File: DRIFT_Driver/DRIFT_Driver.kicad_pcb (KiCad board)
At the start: 2 copper layers, 93 parts, among them IC1 DRV8313RHHR, IC2 DRV8313RHHR, IC4 ESP32-S3-WROOM-1-N4, J1 USB4105-GF-A, J2 Conn_01x04, J3 Conn_01x06, J4 Conn_01x06, J5 Conn_01x04, J6 Conn_01x02, J7 Conn_01x03, J8 Conn_01x03, SW1 SW_SPST, SW2 SW_SPST, U1 74HC32, U2 INA199xxDCK, U3 INA199xxDCK, U4 74HC32, U5 INA199xxDCK, U6 INA199xxDCK, U8 USBLC6-2SC6, U9 MIC5365-3.3YC5

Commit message: Fixed some 3d models
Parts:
- removed the C3 at (124.1, 63.2)
- added C23: 10u, Capacitor_SMD:C_0805_2012Metric, F.Cu at (130.8, 36.9)
- C10: renamed from C18; footprint Capacitor_SMD:C_0402_1005Metric -> Capacitor_SMD:C_0805_2012Metric
- C13: value 22uF -> 10u; footprint Capacitor_SMD:C_0402_1005Metric -> Capacitor_SMD:C_0805_2012Metric
- C2: renamed from C26; footprint Capacitor_SMD:C_0402_1005Metric -> Capacitor_SMD:C_0805_2012Metric
- C6: renamed from C27; footprint Capacitor_SMD:C_0402_1005Metric -> Capacitor_SMD:C_0805_2012Metric
- C9: renamed from C29; footprint Capacitor_SMD:C_0402_1005Metric -> Capacitor_SMD:C_0805_2012Metric
- moved C13 20.0 mm to (131.3, 61.0)
- moved C14 1.43 mm to (124.5, 60.6)
- moved C15 1.43 mm to (127.3, 66.5)
- moved C17 1.43 mm to (127.3, 68.5)
- moved C19 1.43 mm to (124.5, 68.5)
- moved C20 1.43 mm to (127.3, 64.5)
- moved C21 1.43 mm to (124.5, 66.5)
- moved C22 1.43 mm to (127.3, 60.6)
- moved D3 1.43 mm to (124.9, 79.1)
- moved R12 1.43 mm to (113.1, 62.6)
- moved R13 1.43 mm to (113.1, 64.6)
- moved R14 1.43 mm to (113.1, 66.6)
- moved R16 1.43 mm to (110.2, 66.6)
- moved R17 1.43 mm to (110.2, 62.6)
- moved R19 1.43 mm to (110.2, 64.6)
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- renumbered C21 to C1, C24 to C11, C25 to C12, C1 to C14, C12 to C15, C2 to C16, C30 to C17, C8 to C18, C6 to C19, C9 to C20, C5 to C21, C7 to C22, C10 to C24, C14 to C25, C4 to C26, C31 to C27, C11 to C28, C16 to C29, C20 to C3, C19 to C30, C15 to C31, C17 to C32, C32 to C4, C28 to C5, C22 to C7, C23 to C8, D3 to D1, D4 to D2, D1 to D3, D2 to D4, IC4 to IC1, IC1 to IC2, IC2 to IC3, J6 to J1, J3 to J2, J4 to J3, J2 to J4, J7 to J6, J8 to J7, J1 to J8, R28 to R1, R34 to R10, R8 to R11, R10 to R12, R11 to R13, R12 to R14, R1 to R15, R4 to R16, R2 to R17, R5 to R18, R3 to R19, R29 to R2, R6 to R20, R13 to R21, R7 to R22, R9 to R23, R21 to R24, R23 to R25, R24 to R26, R25 to R27, R14 to R28, R17 to R29, R27 to R3, R15 to R30, R18 to R31, R16 to R32, R19 to R33, R26 to R34, R20 to R35, R22 to R36, R35 to R4, R36 to R5, R30 to R6, R31 to R7, R32 to R8, R33 to R9, U9 to U1, U8 to U2, U1 to U3, U2 to U4, U3 to U5, U4 to U6, U5 to U7, U6 to U8
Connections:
- C13 pad 1: VMOT -> GND
- C13 pad 2: GND -> VMOT

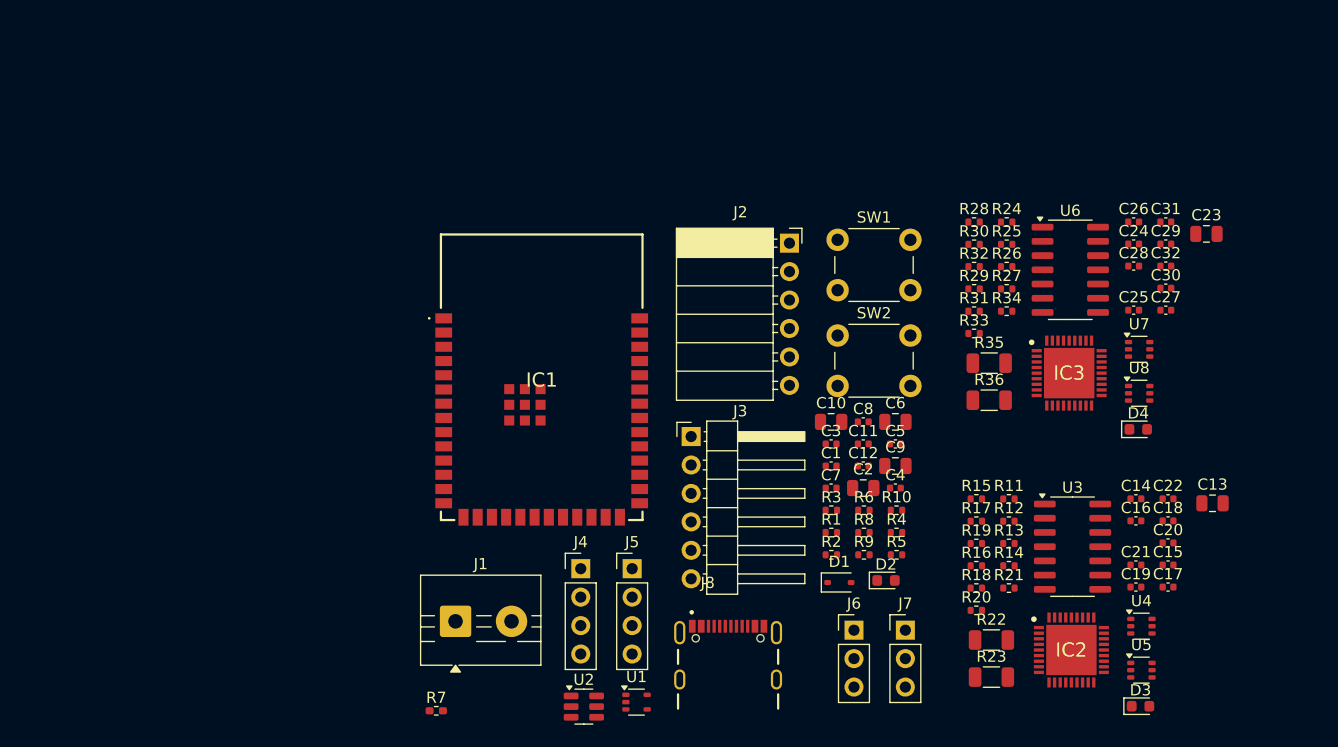
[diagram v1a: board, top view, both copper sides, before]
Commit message: Added second terminal block
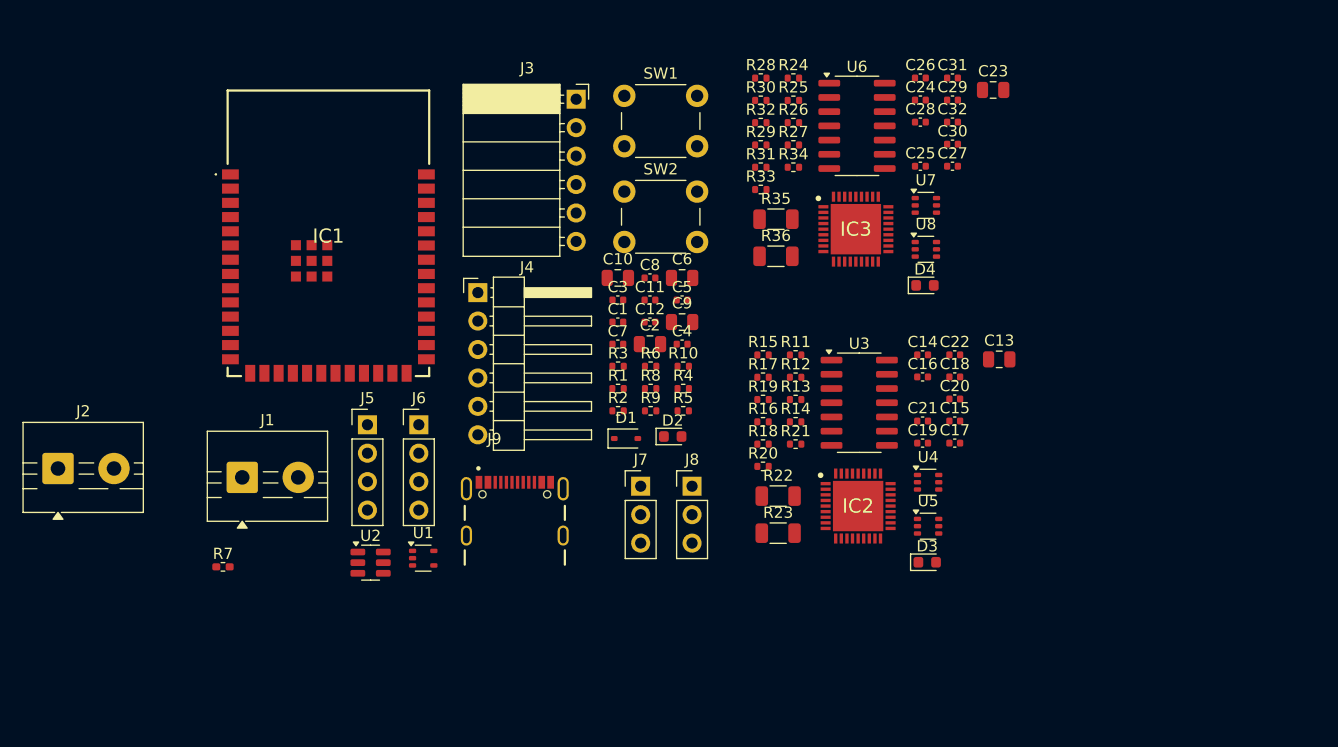
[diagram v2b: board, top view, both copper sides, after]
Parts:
- added J2: Conn_01x02, TerminalBlock:TerminalBlock_MaiXu_MX126-5.0-02P_1x02_P5.00mm, F.Cu at (28.2, 57.9)
- moved C1 23.0 mm to (78.2, 44.8)
- moved C3 23.0 mm to (78.2, 42.8)
- moved C7 23.0 mm to (78.2, 46.8)
- moved C10 23.0 mm to (78.2, 40.9)
- moved C13 23.0 mm to (112.3, 48.1)
- moved J4 23.0 mm to (65.7, 42.2)
- moved C11 23.0 mm to (81.1, 42.8)
- moved C12 23.0 mm to (81.1, 44.8)
- moved C14 23.0 mm to (105.4, 47.7)
- moved C15 23.0 mm to (108.3, 53.7)
- moved C17 23.0 mm to (108.3, 55.6)
- moved C19 23.0 mm to (105.4, 55.6)
- moved C2 23.0 mm to (81.1, 46.8)
- moved C20 23.0 mm to (108.3, 51.7)
- moved C21 23.0 mm to (105.4, 53.7)
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- renumbered J2 to J3, J3 to J4, J4 to J5, J5 to J6, J6 to J7, J7 to J8, J8 to J9

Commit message: Some progress on motor driver unit layout
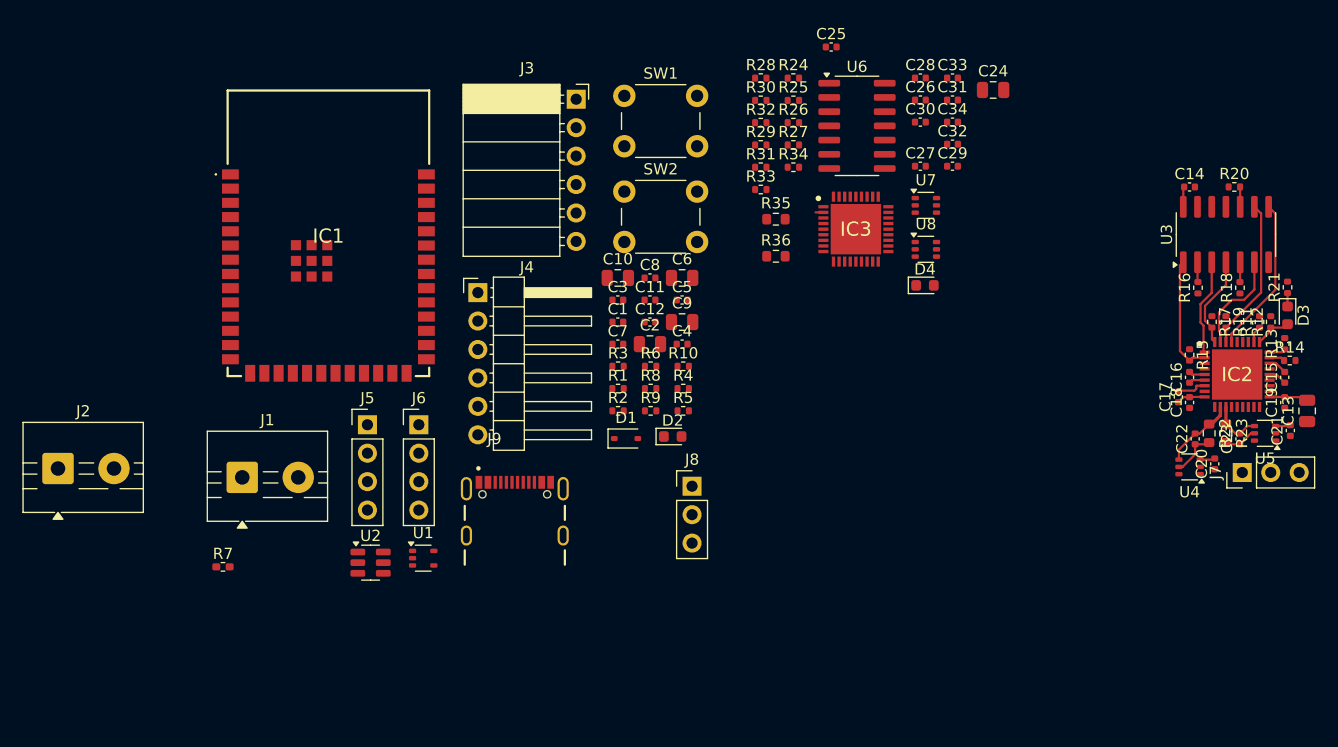
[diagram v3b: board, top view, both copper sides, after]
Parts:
- added C14: 0.1u, Capacitor_SMD:C_0402_1005Metric, F.Cu at (129.2, 32.8)
- added C25: 0.1u, Capacitor_SMD:C_0402_1005Metric, F.Cu at (97.2, 20.2)
- R22, R23, R35, R36: footprint Resistor_SMD:R_1206_3216Metric -> Resistor_SMD:R_0603_1608Metric
- moved J7 53.7 mm to (134.0, 58.2), turned to 90 degrees
- moved R20 48.9 mm to (133.2, 32.8)
- moved R21 46.1 mm to (138.0, 41.7), turned to 90 degrees
- moved R18 44.8 mm to (133.8, 41.8), turned to 90 degrees
- moved R14 44.5 mm to (138.2, 48.2)
- moved R13 44.0 mm to (137.8, 46.8), turned to 90 degrees
- moved R12 42.7 mm to (136.5, 44.8), turned to 90 degrees
- moved R19 41.9 mm to (132.5, 44.8), turned to -90 degrees
- moved R11 41.5 mm to (135.5, 44.8), turned to 90 degrees
- moved R23 41.0 mm to (132.5, 54.8), turned to -90 degrees
- moved R16 40.6 mm to (130.0, 41.8), turned to 90 degrees
- moved R17 40.4 mm to (131.2, 44.8), turned to -90 degrees
- moved D3 39.0 mm to (138.0, 44.2), turned to -90 degrees
- moved R22 38.9 mm to (131.0, 54.8), turned to -90 degrees
- moved R15 38.1 mm to (129.2, 47.8), turned to -90 degrees
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- renumbered C14 to C15, C15 to C16, C16 to C17, C17 to C18, C18 to C19, C19 to C20, C20 to C21, C21 to C22, C22 to C23, C23 to C24, C24 to C26, C25 to C27, C26 to C28, C27 to C29, C28 to C30, C29 to C31, C30 to C32, C31 to C33, C32 to C34
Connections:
- IC1 pad 12: unconnected-(IC1-IO8-Pad12) -> /IN2HA
- IC1 pad 15: unconnected-(IC1-IO3-Pad15) -> /IN2LA
- IC1 pad 16: unconnected-(IC1-IO46-Pad16) -> /IN3HA
- IC1 pad 17: unconnected-(IC1-IO9-Pad17) -> /IN3LA
- IC1 pad 18: unconnected-(IC1-IO10-Pad18) -> /IN1HB
- IC1 pad 19: unconnected-(IC1-IO11-Pad19) -> /IN1LB
- IC1 pad 23: unconnected-(IC1-IO21-Pad23) -> /IN2HB
- IC1 pad 24: unconnected-(IC1-IO47-Pad24) -> /IN2LB
- IC1 pad 25: unconnected-(IC1-IO48-Pad25) -> /IN3HB
- IC1 pad 26: unconnected-(IC1-IO45-Pad26) -> /IN3LB
- IC1 pad 7: unconnected-(IC1-IO7-Pad7) -> /IN1HA
- IC1 pad 9: unconnected-(IC1-IO16-Pad9) -> /IN1LA
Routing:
- net /Driver_Unit/EN3: track 0.00 -> 13.9 mm
- net /IN3HA: track 0.00 -> 13.6 mm
- net /IN1HA: track 0.00 -> 10.7 mm
- net /Driver_Unit/EN2: track 0.00 -> 9.13 mm
- net GND: track 0.00 -> 8.80 mm
- net /Driver_Unit/EN1: track 0.00 -> 8.59 mm
- net /IN2HA: track 0.00 -> 8.26 mm
- net /Driver_Unit/SGND1: track 0.00 -> 6.60 mm
- net +3.3V: track 0.00 -> 6.15 mm
- net VMOT: track 0.00 -> 6.02 mm
- net /Driver_Unit/SGND2: track 0.00 -> 4.70 mm
- net /Driver_Unit/FAULT: track 0.00 -> 3.33 mm
- net Net-(IC2-VCP): track 0.00 -> 2.70 mm
- net /IN1LA: track 0.00 -> 1.78 mm
- net /IN3LA: track 0.00 -> 1.78 mm
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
